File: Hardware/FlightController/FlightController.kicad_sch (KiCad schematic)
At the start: 0 parts

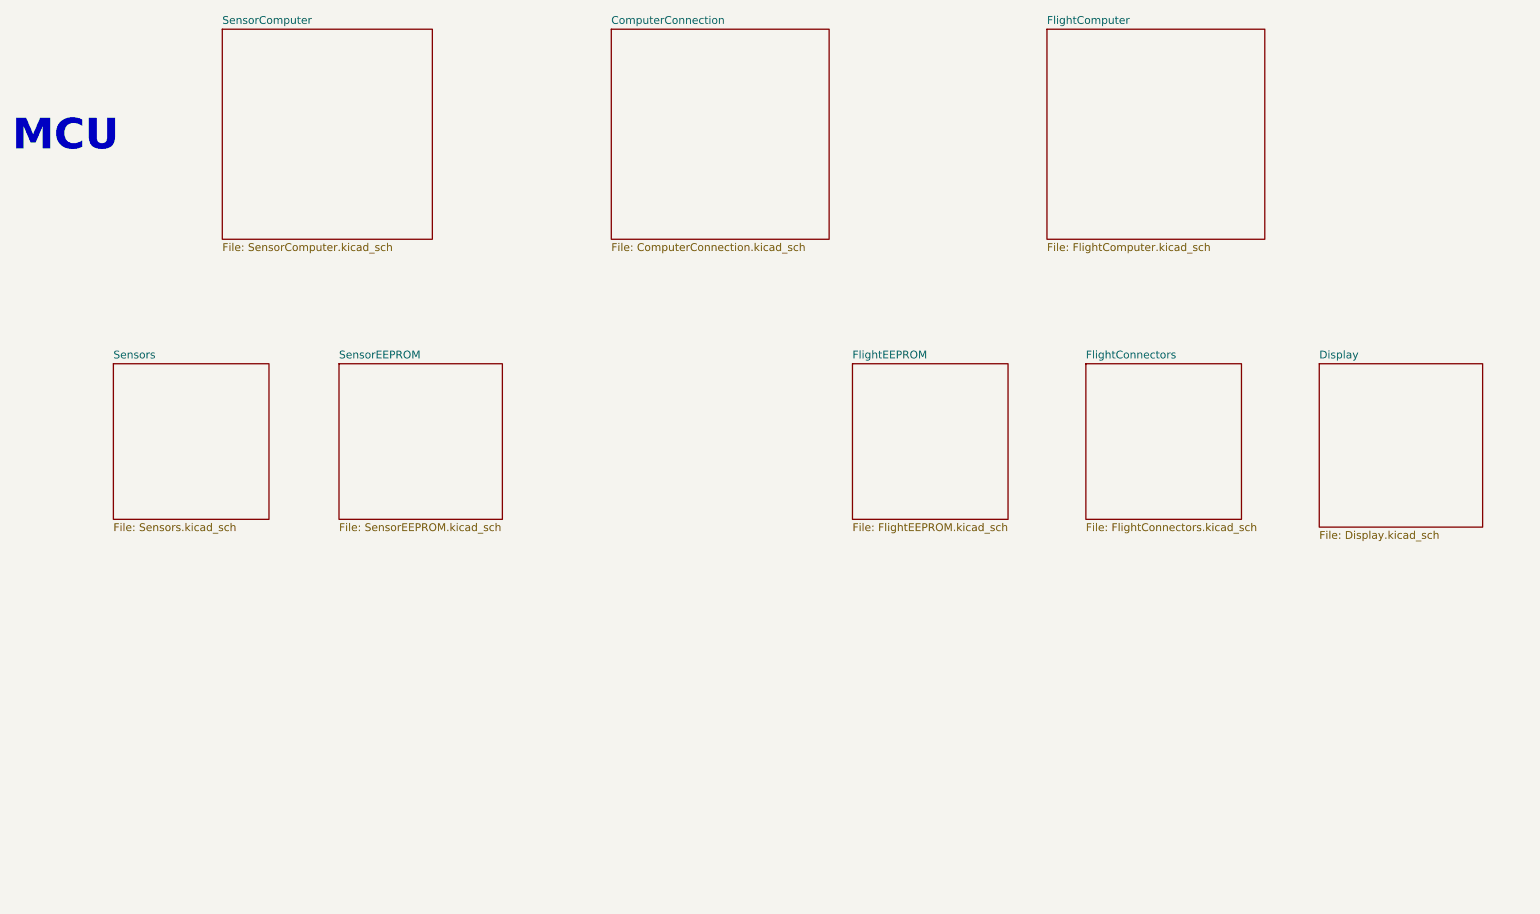
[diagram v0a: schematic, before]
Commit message: Add Sensor MCU schematic items
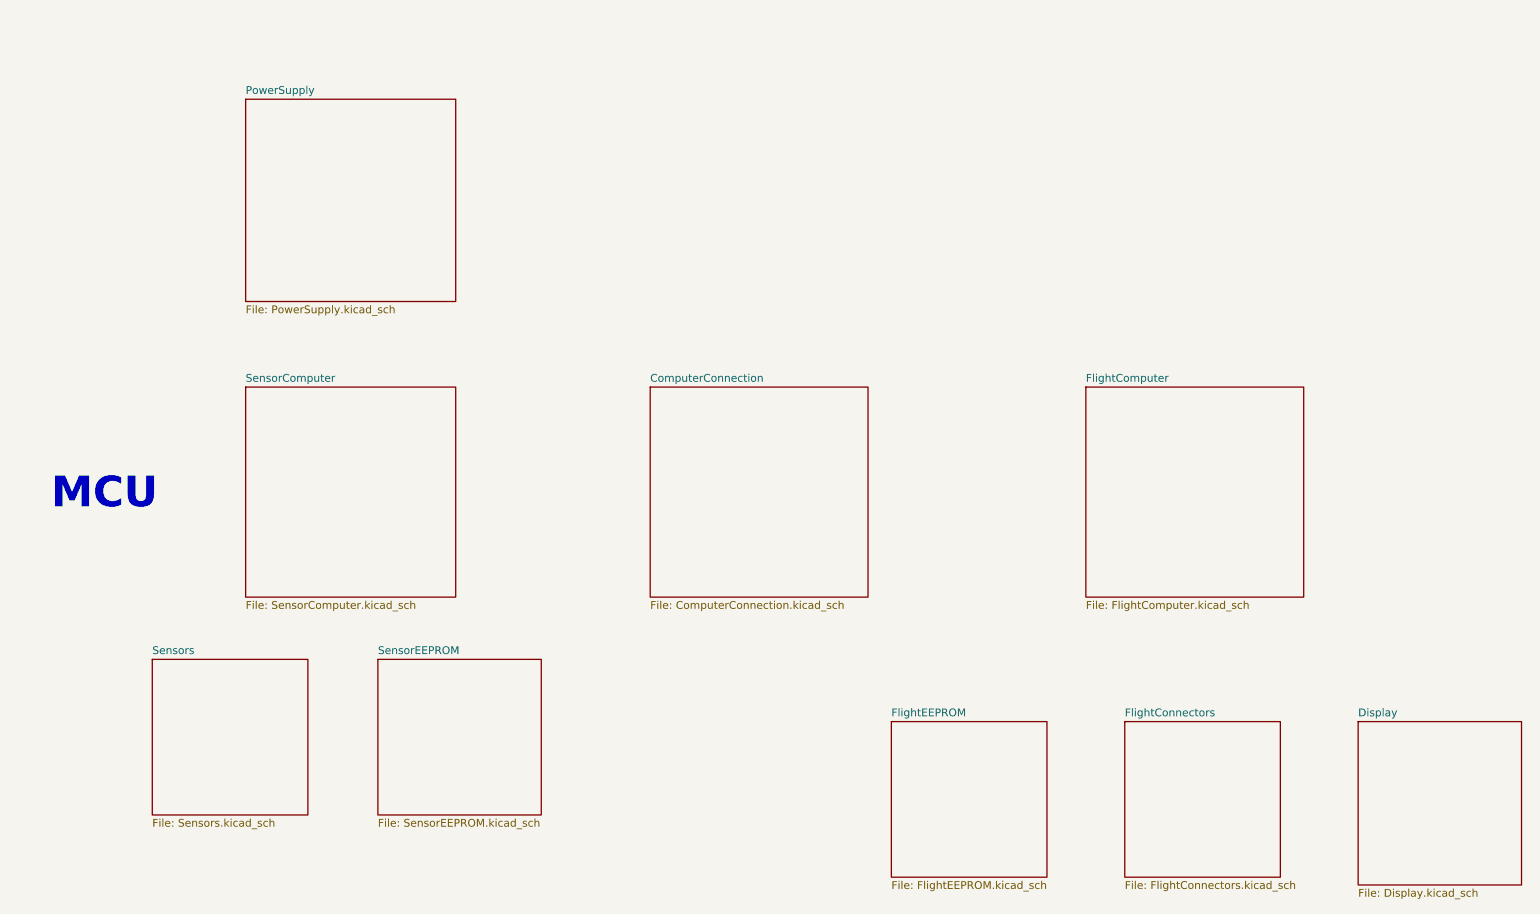
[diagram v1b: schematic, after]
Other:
- added sheet PowerSupply (PowerSupply.kicad_sch)

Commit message: Add ICM-42670-P symbol and schematic
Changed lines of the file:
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@@
     )
   )
-  (sheet (at 81.28 124.46) (size 26.67 25.4) (fields_autoplaced)
-    (stroke (width 0.1524) (type solid) (color 0 0 0 0))
-    (fill (color 0 0 0 0.0000))
-    (property "Sheet name" "SensorEEPROM" (id 0) (at 81.28 123.7484 0)
-      (effects (font (size 1.27 1.27)) (justify left bottom))
-    )
-    (property "Sheet file" "SensorEEPROM.kicad_sch" (id 1) (at 81.28 150.4446 0)
+  (sheet (at 81.28 134.62) (size 26.67 25.4) (fields_autoplaced)
+    (stroke (width 0.1524) (type solid) (color 0 0 0 0))
+    (fill (color 0 0 0 0.0000))
+    (property "Sheet name" "SensorEEPROM" (id 0) (at 81.28 133.9084 0)
+      (effects (font (size 1.27 1.27)) (justify left bottom))
+    )
+    (property "Sheet file" "SensorEEPROM.kicad_sch" (id 1) (at 81.28 160.6046 0)
       (effects (font (size 1.27 1.27)) (justify left top))
     )
@@
     )
   )
-  (sheet (at 59.69 33.02) (size 34.29 33.02) (fields_autoplaced)
-    (stroke (width 0.1524) (type solid) (color 0 0 0 0))
-    (fill (color 0 0 0 0.0000))
-    (property "Sheet name" "PowerSupply" (id 0) (at 59.69 32.3084 0)
-      (effects (font (size 1.27 1.27)) (justify left bottom))
-    )
-    (property "Sheet file" "PowerSupply.kicad_sch" (id 1) (at 59.69 66.6246 0)
+  (sheet (at 125.73 30.48) (size 35.56 33.02) (fields_autoplaced)
+    (stroke (width 0.1524) (type solid) (color 0 0 0 0))
+    (fill (color 0 0 0 0.0000))
+    (property "Sheet name" "PowerSupply" (id 0) (at 125.73 29.7684 0)
+      (effects (font (size 1.27 1.27)) (justify left bottom))
+    )
+    (property "Sheet file" "PowerSupply.kicad_sch" (id 1) (at 125.73 64.0846 0)
       (effects (font (size 1.27 1.27)) (justify left top))
     )
@@
     )
   )
-  (sheet (at 44.45 124.46) (size 25.4 25.4) (fields_autoplaced)
-    (stroke (width 0.1524) (type solid) (color 0 0 0 0))
-    (fill (color 0 0 0 0.0000))
-    (property "Sheet name" "Sensors" (id 0) (at 44.45 123.7484 0)
-      (effects (font (size 1.27 1.27)) (justify left bottom))
-    )
-    (property "Sheet file" "Sensors.kicad_sch" (id 1) (at 44.45 150.4446 0)
+  (sheet (at 44.45 134.62) (size 25.4 25.4) (fields_autoplaced)
+    (stroke (width 0.1524) (type solid) (color 0 0 0 0))
+    (fill (color 0 0 0 0.0000))
+    (property "Sheet name" "Sensors" (id 0) (at 44.45 133.9084 0)
+      (effects (font (size 1.27 1.27)) (justify left bottom))
+    )
+    (property "Sheet file" "Sensors.kicad_sch" (id 1) (at 44.45 160.6046 0)
       (effects (font (size 1.27 1.27)) (justify left top))
     )
@@
       (reference "#PWR017") (unit 1) (value "+3.3VA") (footprint "")
     )
+    (path "/4354cbd2-e9c4-4e30-9827-d99ebbfc8118/5e42f8a6-d5d0-417f-add5-3c2cbcde8da4"
+      (reference "#PWR018") (unit 1) (value "+3.3V") (footprint "")
+    )
+    (path "/4354cbd2-e9c4-4e30-9827-d99ebbfc8118/10753d65-64b0-4eea-bb13-7ab064a80423"
+      (reference "#PWR019") (unit 1) (value "+3.3V") (footprint "")
+    )
+    (path "/4354cbd2-e9c4-4e30-9827-d99ebbfc8118/e7fbf42f-4c47-4ed5-be61-c221d43108c3"
+      (reference "#PWR020") (unit 1) (value "+3.3V") (footprint "")
+    )
+    (path "/4354cbd2-e9c4-4e30-9827-d99ebbfc8118/7d83d908-d3a4-474b-97bb-e6b0713f696d"
+      (reference "#PWR021") (unit 1) (value "GND") (footprint "")
+    )
+    (path "/beafb0fa-bc5a-45f7-a671-ae1fea1f5da0/643b7a9e-b43c-4525-a889-168b259c28a0"
+      (reference "#PWR022") (unit 1) (value "+3.3V") (footprint "")
+    )
+    (path "/beafb0fa-bc5a-45f7-a671-ae1fea1f5da0/52966bb4-3197-4eca-8645-f5ad76297ed2"
+      (reference "#PWR023") (unit 1) (value "GND") (footprint "")
+    )
+    (path "/beafb0fa-bc5a-45f7-a671-ae1fea1f5da0/61a532e1-447a-4194-ba4f-1963e96282ae"
+      (reference "#PWR024") (unit 1) (value "GND") (footprint "")
+    )
+    (path "/beafb0fa-bc5a-45f7-a671-ae1fea1f5da0/4b6dc1c0-5445-4e53-ae26-80eed81beb4c"
+      (reference "#PWR025") (unit 1) (value "GND") (footprint "")
+    )
+    (path "/beafb0fa-bc5a-45f7-a671-ae1fea1f5da0/050e6b57-8c1f-49ed-87c6-57ef4274e569"
+      (reference "#PWR026") (unit 1) (value "GND") (footprint "")
+    )
+    (path "/beafb0fa-bc5a-45f7-a671-ae1fea1f5da0/ec1e020b-2db3-4803-bb06-d189b615dcea"
+      (reference "#PWR027") (unit 1) (value "+3.3V") (footprint "")
+    )
     (path "/4354cbd2-e9c4-4e30-9827-d99ebbfc8118/8f660c2e-10ea-4177-ac19-0f38c3f32fe7"
       (reference "#PWR0101") (unit 1) (value "GND") (footprint "")
@@
       (reference "#PWR0111") (unit 1) (value "GND") (footprint "")
     )
+    (path "/26011f71-4e3a-4961-9d66-e0f899aae2bd/3d24cb55-207e-4375-b07f-7dcf98f81a8f"
+      (reference "#PWR?") (unit 1) (value "GND") (footprint "")
+    )
+    (path "/26011f71-4e3a-4961-9d66-e0f899aae2bd/6449bfbf-9aa2-4f24-bc37-5fa5f8b6bfab"
+      (reference "#PWR?") (unit 1) (value "+3.3V") (footprint "")
+    )
     (path "/8a0d5691-062e-42a2-ae62-fa37b063f597/2a7d6eea-6000-42a2-8256-e0dc52fb8c7c"
       (reference "C1") (unit 1) (value "4.7uF") (footprint "Capacitor_SMD:C_0603_1608Metric")
@@
       (reference "C17") (unit 1) (value "10nF") (footprint "Capacitor_SMD:C_0603_1608Metric")
     )
+    (path "/beafb0fa-bc5a-45f7-a671-ae1fea1f5da0/57e54a4a-5f4c-46f1-9110-c8e9475fc579"
+      (reference "C18") (unit 1) (value "10nF") (footprint "Capacitor_SMD:C_0603_1608Metric")
+    )
+    (path "/beafb0fa-bc5a-45f7-a671-ae1fea1f5da0/6c35333a-6e6a-4438-9954-212361236691"
+      (reference "C19") (unit 1) (value "0.1uF") (footprint "Capacitor_SMD:C_0603_1608Metric")
+    )
+    (path "/beafb0fa-bc5a-45f7-a671-ae1fea1f5da0/e6546842-aa76-4fe7-a80e-dea05b124777"
+      (reference "C20") (unit 1) (value "2.2uF") (footprint "Capacitor_SMD:C_0603_1608Metric")
+    )
     (path "/8a0d5691-062e-42a2-ae62-fa37b063f597/d2ce6b0a-e5d9-44a8-82d9-4f12095b88b0"
       (reference "D1") (unit 1) (value "RED") (footprint "LED_SMD:LED_0603_1608Metric")
     )
+    (path "/8a0d5691-062e-42a2-ae62-fa37b063f597/e5138f28-e7c9-444d-ab74-597ec6b89d50"
+      (reference "F1") (unit 1) (value "750mA") (footprint "")
+    )
     (path "/8a0d5691-062e-42a2-ae62-fa37b063f597/b6d56f24-66ca-48ce-a62a-724b505f5dc3"
       (reference "J1") (unit 1) (value "Conn_01x02") (footprint "")
@@
       (reference "J4") (unit 1) (value "Conn_02x03_Odd_Even") (footprint "")
     )
+    (path "/4354cbd2-e9c4-4e30-9827-d99ebbfc8118/33ebcdc3-2236-4647-a389-0c8248cd3c4c"
+      (reference "J5") (unit 1) (value "Conn_01x04") (footprint "")
+    )
     (path "/8a0d5691-062e-42a2-ae62-fa37b063f597/88dd039d-dd4f-4b21-a1b3-bba0726cb4ff"
       (reference "L1") (unit 1) (value "8.2 uH") (footprint "")
@@
     )
     (path "/8a0d5691-062e-42a2-ae62-fa37b063f597/45e09f42-0d40-4748-b8e2-597f1eedf9de"
-      (reference "R7") (unit 1) (value "1.5k") (footprint "Resistor_SMD:R_0603_1608Metric")
+      (reference "R7") (unit 1) (value "1k") (footprint "Resistor_SMD:R_0603_1608Metric")
+    )
+    (path "/4354cbd2-e9c4-4e30-9827-d99ebbfc8118/d2029644-74fa-4e9c-87aa-fc5793e7017a"
+      (reference "R8") (unit 1) (value "2.2k") (footprint "Resistor_SMD:R_0603_1608Metric")
+    )
+    (path "/4354cbd2-e9c4-4e30-9827-d99ebbfc8118/4f57e901-fc98-437e-b673-0ef6702ed715"
+      (reference "R9") (unit 1) (value "2.2k") (footprint "Resistor_SMD:R_0603_1608Metric")
     )
     (path "/4354cbd2-e9c4-4e30-9827-d99ebbfc8118/2a646e65-3efb-4e20-8205-2e84f7895314"
@@
       (reference "U3") (unit 1) (value "LMR54410DBVR") (footprint "Package_TO_SOT_SMD:SOT-23-6")
     )
+    (path "/beafb0fa-bc5a-45f7-a671-ae1fea1f5da0/787af3ff-5d20-4564-bb94-cafd3ab19d75"
+      (reference "U4") (unit 1) (value "ICM-42670-P") (footprint "Package_LGA:LGA-14_3x2.5mm_P0.5mm_LayoutBorder3x4y")
+    )
     (path "/4354cbd2-e9c4-4e30-9827-d99ebbfc8118/3b5099b2-2cdf-44df-9ac9-85364c6a641f"

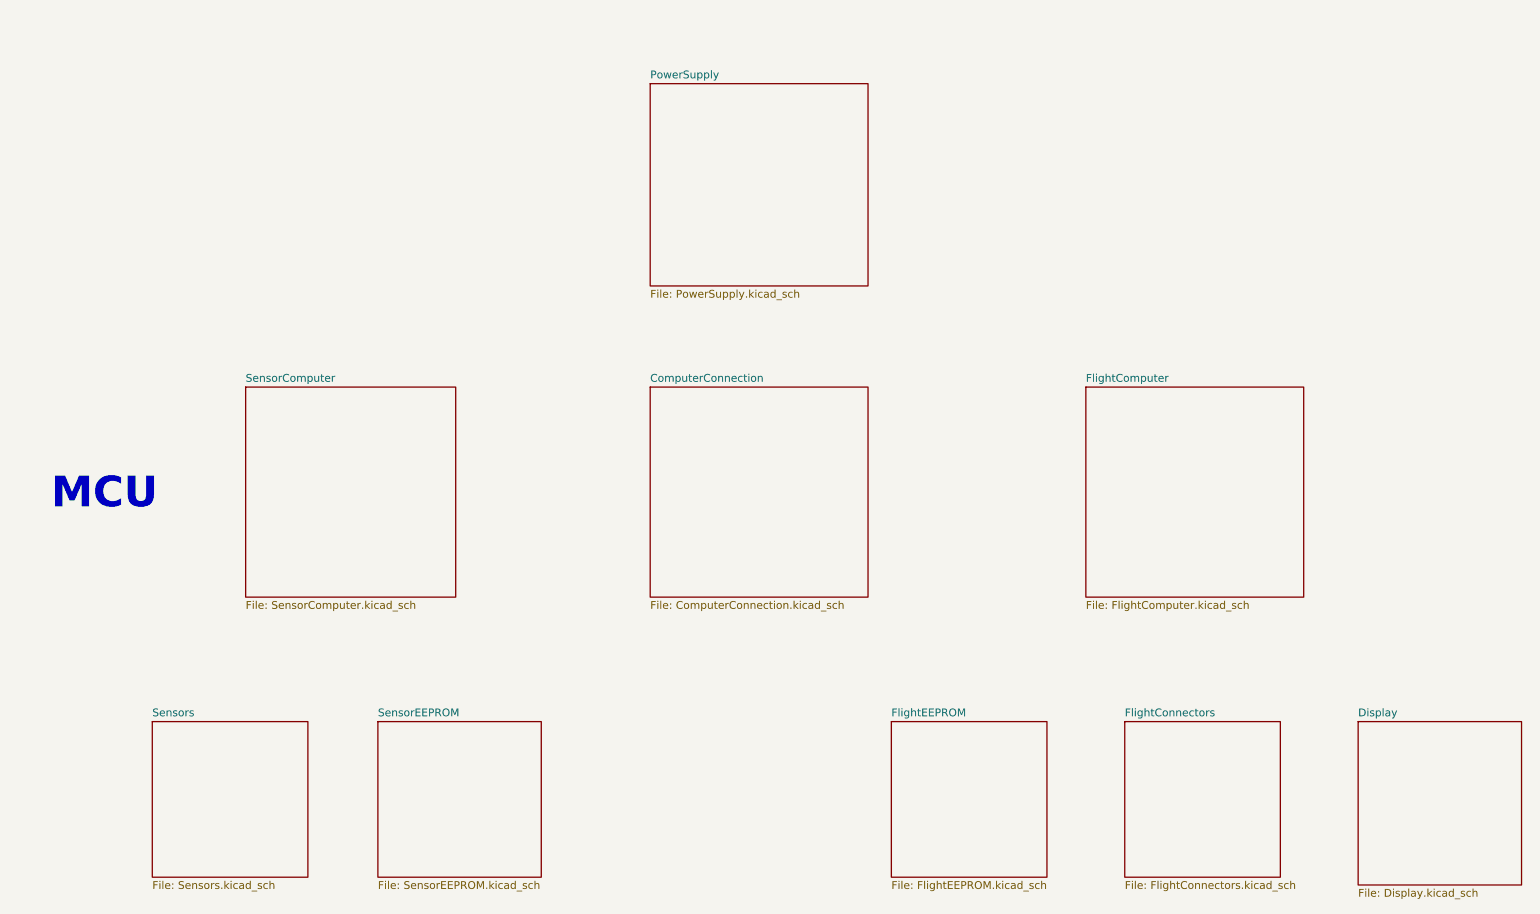
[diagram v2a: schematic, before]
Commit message: Round out basic schematic and add preliminary board layout
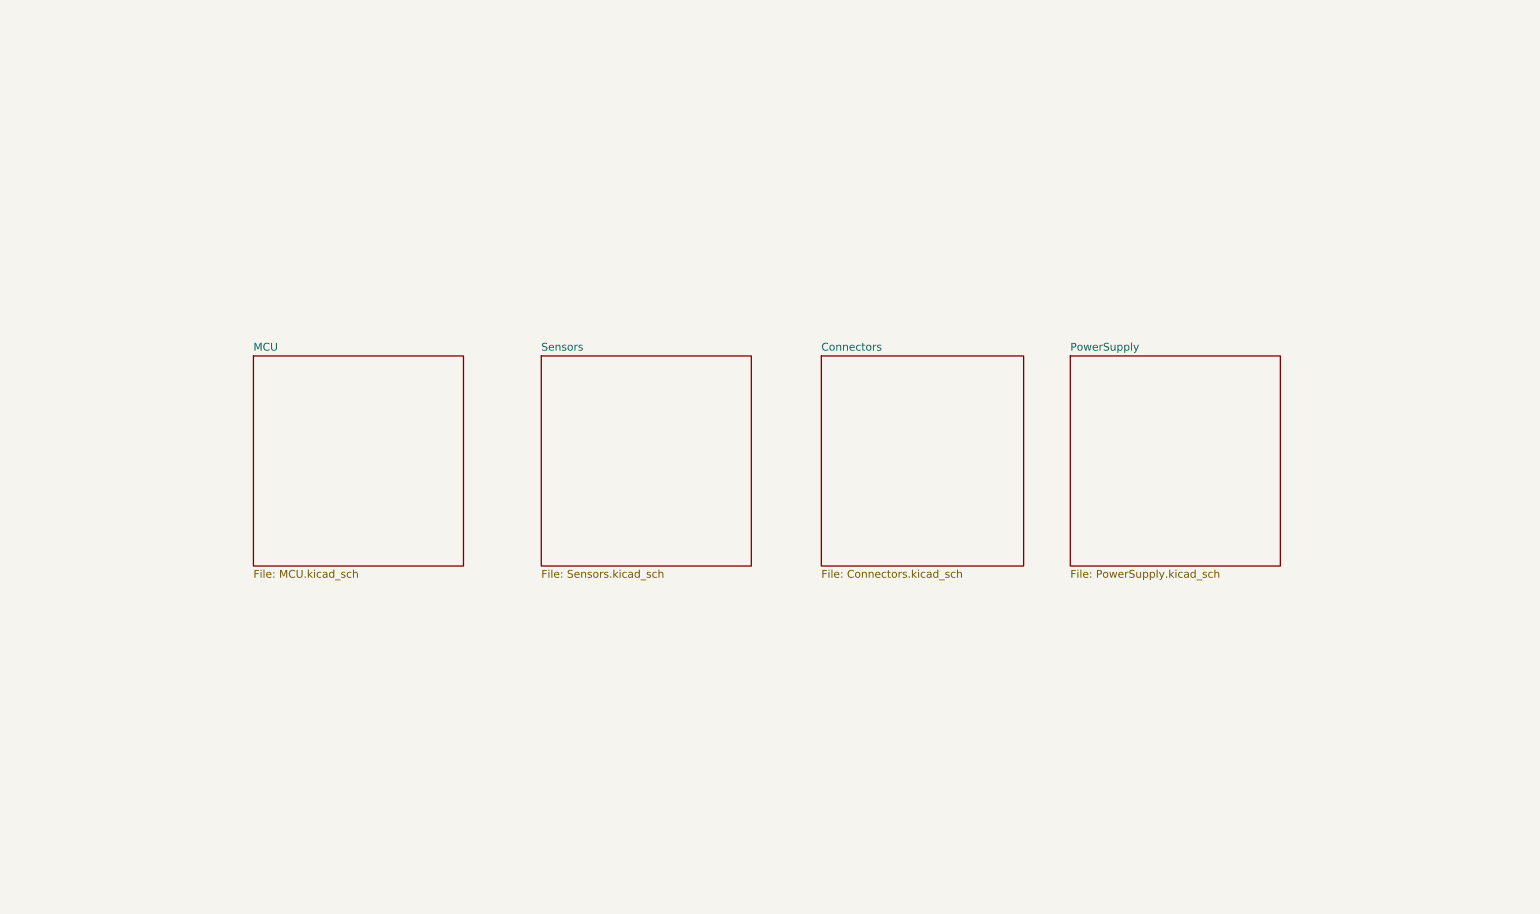
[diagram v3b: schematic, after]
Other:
- sheet SensorComputer renamed MCU
- removed sheet ComputerConnection
- removed sheet Display
- removed sheet FlightComputer
- removed sheet FlightConnectors
- removed sheet FlightEEPROM
- removed sheet SensorEEPROM
- added sheet Connectors (Connectors.kicad_sch)
- sheet MCU: file SensorComputer.kicad_sch -> MCU.kicad_sch
- note removed: "MCU"
